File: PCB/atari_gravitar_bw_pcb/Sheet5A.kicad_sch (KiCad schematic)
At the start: 0 parts

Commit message: Worked on sheet 5A
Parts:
- added B_3, C/D_3: POKEY, symbol atari:POKEY
- added B_4, D_4: SW_DIP_x08, symbol Switch:SW_DIP_x08
- added B_5, D_5: LM324, symbol Amplifier_Operational:LM324
- added C27, C28: .001, symbol Device:C
- added C29, C35: .1, symbol Device:C
- added C30, C33, C34: .22, symbol Device:C
- added C31, C32: .015, symbol Device:C
- added C39: 10uf 50v, symbol Device:C_Polarized_US
- added C44: .01, symbol Device:C
- added R24, R25, R26, R27, R28, R29, R30, R31, R32, R33, R34, R35, R36, R37, R38, R39, R46: 10k, symbol Device:R_US
- added R43, R44, R48: 1m, symbol Device:R_US
- added R45, R50: 100k, symbol Device:R_US
- added R47, R51: 1k, symbol Device:R_US
- added R49, R52: 3.9k, symbol Device:R_US
- added R53, R54: 3.3k, symbol Device:R_US
- added TPAUD1, TPAUD2: tp_2_pin, symbol atari:tp_2_pin
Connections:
- new net: B_5.9 (-), R46.1, R49.2, R52.1
- new net: C28.2, D_5.1, R44.2, R46.2
- new net: C27.1, D_5.6 (-), R43.1, R45.2
- new net: C27.2, D_5.7, R43.2, R48.1
- new net: B_5.6 (-), C/D_3.37 (OUT), C31.1, C34.1, R51.1
- new net: B_5.7, C33.1, C34.2, R51.2
- new net: B_5.2 (-), B_5.8, R52.2, R53.1
- new net: C/D_3.9 (P7), D_4.1, R31.2
- new net: B_3.14 (P0), B_4.8, R33.2
- new net: B_3.11 (P5), B_4.3, R36.2
- new net: C/D_3.10 (P4), D_4.4, R28.2
- new net: C/D_3.11 (P5), D_4.3, R29.2
- new net: C/D_3.12 (P2), D_4.6, R26.2
- new net: C/D_3.13 (P3), D_4.5, R27.2
- new net: C/D_3.14 (P0), D_4.8, R24.2
- new net: C/D_3.15 (P1), D_4.7, R25.2
- new net: C/D_3.8 (P6), D_4.2, R30.2
- new net: B_3.15 (P1), B_4.7, R32.2
- new net: C30.1, D_5.8, R47.2
- new net: C30.2, R45.1
- new net: B_3.10 (P4), B_4.4, R37.2
- new net: B_3.12 (P2), B_4.6, R35.2
- new net: B_3.13 (P3), B_4.5, R34.2
- new net: B_3.37 (OUT), C32.1, D_5.9 (-), R47.1
- new net: B_3.8 (P6), B_4.2, R39.2
- new net: B_3.9 (P7), B_4.1, R38.2
- new net: C33.2, R49.1
- new net: C28.1, D_5.2 (-), R44.1, R48.2
- new net: B_5.5 (+), C39.1, C44.1, D_5.10 (+), R50.2
- new net: B_5.13 (-), R53.2, R54.1
- new net +15V: B_5.4 (V+), C29.1, C35.1, D_5.4 (V+)
- new net +5V: B_3.17 (VCC), C/D_3.17 (VCC), R24.1, R25.1, R26.1, R27.1, R28.1, R29.1, R30.1, R31.1, R32.1, R33.1, R34.1, R35.1, R36.1, R37.1, R38.1, R39.1, R50.1
- new net -15V: B_5.11 (V-)
- new net AB0: B_3.36 (A0), C/D_3.36 (A0)
- new net AB1: B_3.35 (A1), C/D_3.35 (A1)
- new net AB2: B_3.34 (A2), C/D_3.34 (A2)
- new net AB3: B_3.33 (A3), C/D_3.33 (A3)
- new net AUD1: B_5.14, R54.2, TPAUD1.1, TPAUD1.2
- new net AUD2: B_5.1, B_5.3 (+), TPAUD2.1, TPAUD2.2
- new net BPHI2: B_3.7 (PHI2), C/D_3.7 (PHI2)
- new net D0: B_3.38 (D0), C/D_3.38 (D0)
- new net D1: B_3.39 (D1), C/D_3.39 (D1)
- new net D2: B_3.40 (D2), C/D_3.40 (D2)
- new net D3: B_3.2 (D3), C/D_3.2 (D3)
- new net D4: B_3.3 (D4), C/D_3.3 (D4)
- new net D5: B_3.4 (D5), C/D_3.4 (D5)
- new net D6: B_3.5 (D6), C/D_3.5 (D6)
- new net D7: B_3.6 (D7), C/D_3.6 (D7)
- new net GND: B_3.1 (GND), B_4.10, B_4.11, B_4.12, B_4.13, B_4.14, B_4.15, B_4.16, B_4.9, B_5.10 (+), B_5.12 (+), C/D_3.1 (GND), C29.2, C31.2, C32.2, C35.2, C39.2, C44.2, D_4.10, D_4.11, D_4.12, D_4.13, D_4.14, D_4.15, D_4.16, D_4.9, D_5.11 (V-), D_5.3 (+), D_5.5 (+)
- new net PR23: B_3.31 (CS1), C/D_3.31 (CS1)
- new net R~{W}B: B_3.32 (R~{W}), C/D_3.32 (R~{W})
- new net ~{IO1}: B_3.30 (~{CS0}), C/D_3.30 (~{CS0})
- no-connect marks 0 -> 26
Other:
- note added: "OPTION SWITCH INPUT AND AUDIO OUTPUT"

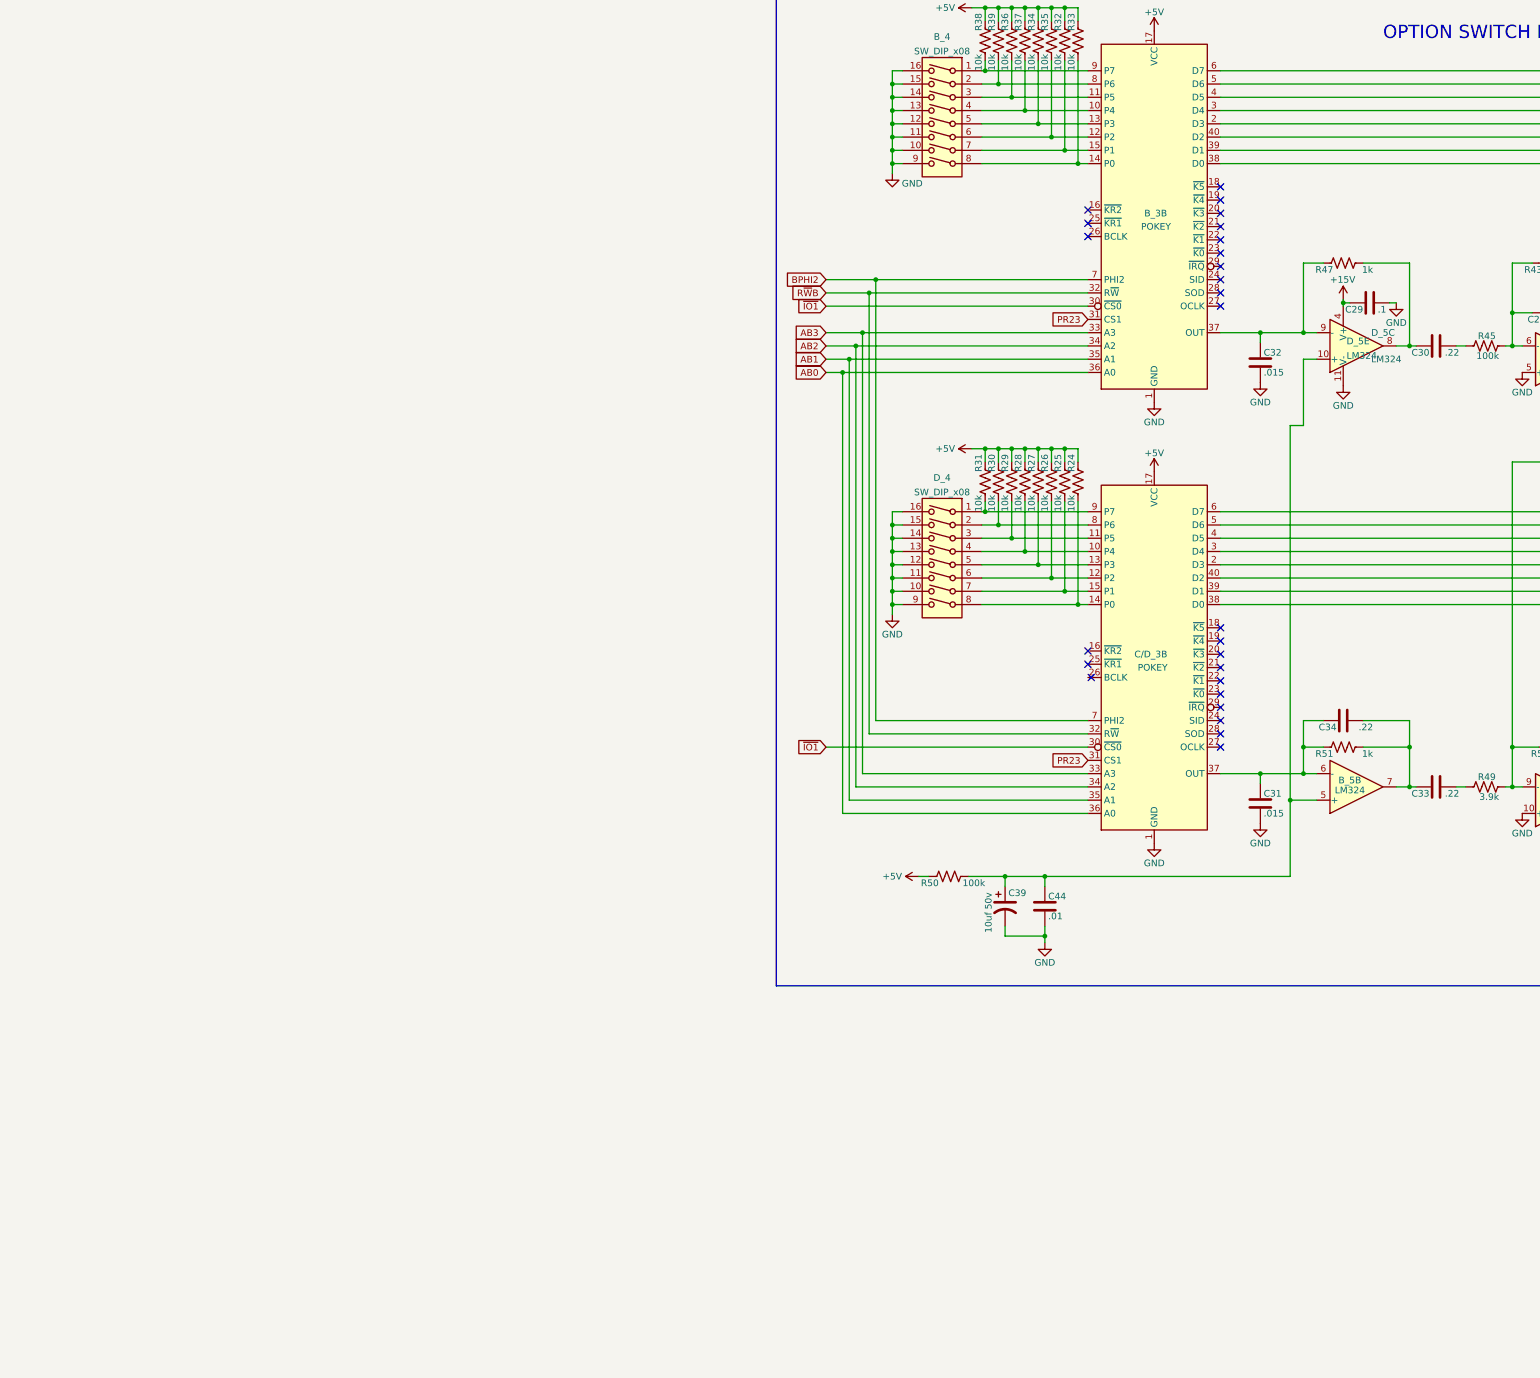
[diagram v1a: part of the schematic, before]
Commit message: Finished sheet 5A
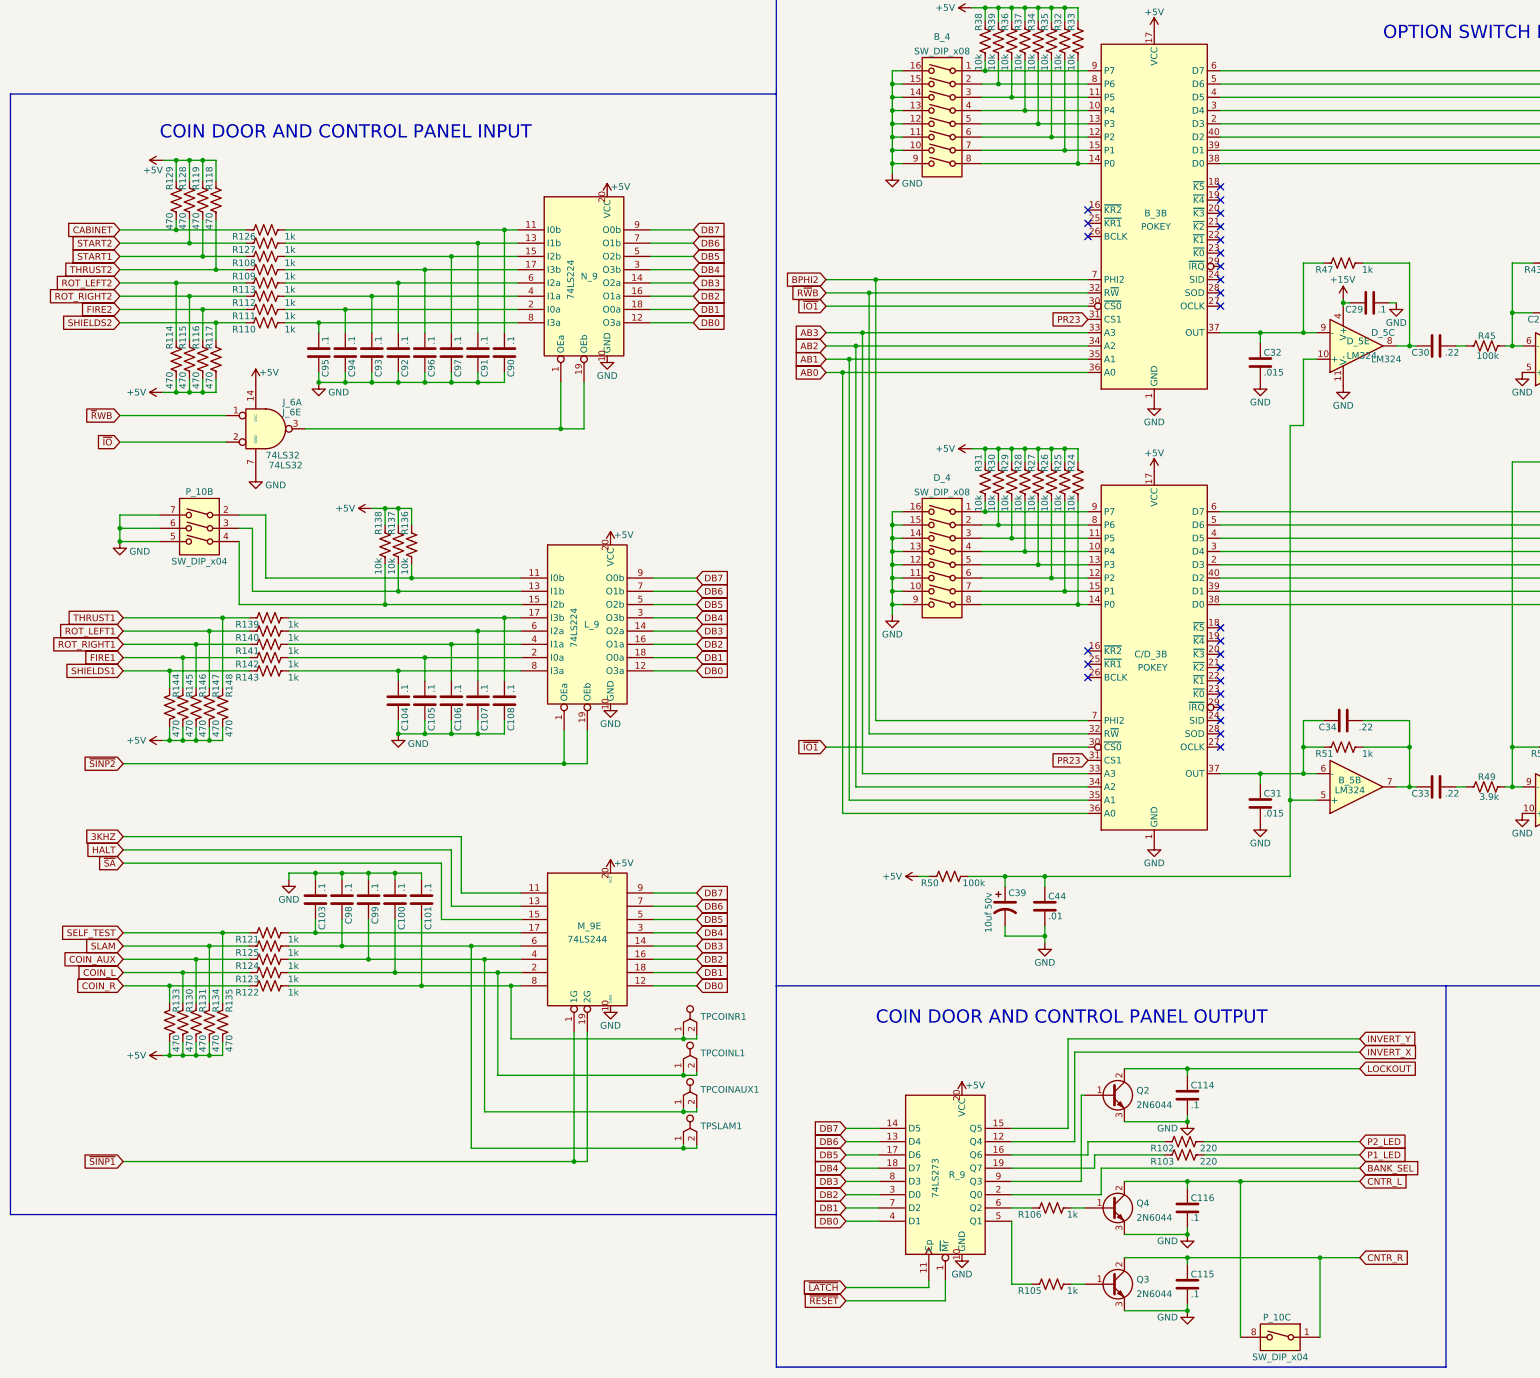
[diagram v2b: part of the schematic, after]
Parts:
- added C100, C101, C103, C104, C105, C106, C107, C108, C114, C115, C116, C90, C91, C92, C93, C94, C95, C96, C97, C98, C99: .1, symbol Device:C
- added J_6: 74LS32, symbol atari:74LS32
- added L_9, N_9: 74LS224, symbol atari:74LS224
- added M_9: 74LS244, symbol atari:74LS244
- added P_10: SW_DIP_x04, symbol atari:SW_DIP_x04
- added Q2, Q3, Q4: 2N6044, symbol Device:Q_NPN_BCE
- added R102, R103: 220, symbol Device:R_US
- added R105, R106, R108, R109, R110, R111, R112, R113, R121, R122, R123, R124, R125, R126, R127, R139, R140, R141, R142, R143: 1k, symbol Device:R_US
- added R114, R115, R116, R117, R118, R119, R128, R129, R130, R131, R133, R134, R135, R144, R145, R146, R147, R148: 470, symbol Device:R_US
- added R136, R137, R138: 10k, symbol Device:R_US
- added R_9: 74LS273, symbol atari:74LS273
- added TPCOINAUX1, TPCOINL1, TPCOINR1, TPSLAM1: tp_2_pin, symbol atari:tp_2_pin
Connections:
- net +5V: now also J_6.14 (VCC), L_9.20 (VCC), M_9.20 (VCC), N_9.20 (VCC), R114.2, R115.2, R116.2, R117.2, R118.1, R119.1, R128.1, R129.1, R130.2, R131.2, R133.2, R134.2, R135.2, R136.1, R137.1, R138.1, R144.2, R145.2, R146.2, R147.2, R148.2, R_9.20 (VCC)
- net GND: now also C100.2, C101.2, C103.2, C104.1, C105.1, C106.1, C107.1, C108.1, C114.2, C115.2, C116.2, C90.1, C91.1, C92.1, C93.1, C94.1, C95.1, C96.1, C97.1, C98.2, C99.2, J_6.7 (GND), L_9.10 (GND), M_9.10 (GND), N_9.10 (GND), P_10.5, P_10.6, P_10.7, Q2.3 (E), Q3.3 (E), Q4.3 (E), R_9.10 (GND)
- new net: L_9.11 (I0b), P_10.2, R136.2
- new net: L_9.13 (I1b), P_10.3, R137.2
- new net: L_9.15 (I2b), P_10.4, R138.2
- new net: Q2.1 (B), R_9.9 (Q3)
- new net: R102.1, R_9.16 (Q6)
- new net: R103.1, R_9.19 (Q7)
- new net: R105.1, R_9.5 (Q1)
- new net: R106.1, R_9.6 (Q2)
- new net: C96.2, N_9.17 (I3b), R109.2
- new net: C105.2, L_9.2 (I0a), R142.2
- new net: C108.2, L_9.17 (I3b), R139.2
- new net: C106.2, L_9.4 (I1a), R141.2
- new net: C107.2, L_9.6 (I2a), R140.2
- new net: C104.2, L_9.8 (I3a), R143.2
- new net: C101.1, M_9.8, R122.2, TPCOINR1.1, TPCOINR1.2
- new net: C103.1, M_9.17, R121.2
- new net: C91.2, N_9.13 (I1b), R127.2
- new net: C99.1, M_9.4, R124.2, TPCOINAUX1.1, TPCOINAUX1.2
- new net: C100.1, M_9.2, R123.2, TPCOINL1.1, TPCOINL1.2
- new net: C90.2, N_9.11 (I0b), R126.2
- new net: C97.2, N_9.15 (I2b), R108.2
- new net: C92.2, N_9.6 (I2a), R113.2
- new net: Q4.1 (B), R106.2
- new net: C98.1, M_9.6, R125.2, TPSLAM1.1, TPSLAM1.2
- new net: C94.2, N_9.2 (I0a), R111.2
- new net: Q3.1 (B), R105.2
- new net: C95.2, N_9.8 (I3a), R110.2
- new net: C93.2, N_9.4 (I1a), R112.2
- new net: J_6.3, N_9.1 (OEa), N_9.19 (OEb)
- new net 3KHZ: M_9.11
- new net BANK_SEL: R_9.2 (Q0)
- new net CABINET: R126.1, R129.2
- new net CNTR_L: C116.1, P_10.8, Q4.2 (C)
- new net CNTR_R: C115.1, P_10.1, Q3.2 (C)
- new net COIN_AUX: R124.1, R131.1
- new net COIN_L: R123.1, R130.1
- new net COIN_R: R122.1, R133.1
- new net DB0: L_9.12 (O3a), M_9.12, N_9.12 (O3a), R_9.4 (D1)
- new net DB1: L_9.18 (O0a), M_9.18, N_9.18 (O0a), R_9.7 (D2)
- new net DB2: L_9.16 (O1a), M_9.16, N_9.16 (O1a), R_9.3 (D0)
- new net DB3: L_9.14 (O2a), M_9.14, N_9.14 (O2a), R_9.8 (D3)
- new net DB4: L_9.3 (O3b), M_9.3, N_9.3 (O3b), R_9.18 (D7)
- new net DB5: L_9.5 (O2b), M_9.5, N_9.5 (O2b), R_9.17 (D6)
- new net DB6: L_9.7 (O1b), M_9.7, N_9.7 (O1b), R_9.13 (D4)
- new net DB7: L_9.9 (O0b), M_9.9, N_9.9 (O0b), R_9.14 (D5)
- new net FIRE1: R142.1, R145.1
- new net FIRE2: R111.1, R116.1
- new net HALT: M_9.13
- new net INVERT_X: R_9.12 (Q4)
- new net INVERT_Y: R_9.15 (Q5)
- new net LOCKOUT: C114.1, Q2.2 (C)
- new net P1_LED: R103.2
- new net P2_LED: R102.2
- new net ROT_LEFT1: R140.1, R147.1
- new net ROT_LEFT2: R113.1, R114.1
- new net ROT_RIGHT1: R141.1, R146.1
- new net ROT_RIGHT2: R112.1, R115.1
- new net SELF_TEST: R121.1, R135.1
- new net SHIELDS1: R143.1, R144.1
- new net SHIELDS2: R110.1, R117.1
- new net SLAM: R125.1, R134.1
- new net START1: R108.1, R119.2
- new net START2: R127.1, R128.2
- new net THRUST1: R139.1, R148.1
- new net THRUST2: R109.1, R118.2
- new net ~{IO}: J_6.2
- new net ~{LATCH}: R_9.11 (Cp)
- new net ~{RESET}: R_9.1 (~{Mr})
- new net ~{R}WB: J_6.1
- new net ~{SA}: M_9.15
- new net ~{SINP1}: M_9.1 (1G), M_9.19 (2G)
- new net ~{SINP2}: L_9.1 (OEa), L_9.19 (OEb)
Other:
- note added: "COIN DOOR AND CONTROL PANEL INPUT"
- note added: "COIN DOOR AND CONTROL PANEL OUTPUT"
